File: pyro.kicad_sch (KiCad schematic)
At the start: 34 parts, among them J15 DB141R-2.54-8P-GN, Q1 MJD44H11T4G, Q10 PJM09P30DF, Q11 PJM09P30DF, Q12 PJM09P30DF, Q13 PJM09P30DF, Q4 BC817-25,215, Q5 NMOS, Q6 NMOS, Q7 NMOS, Q8 NMOS, Q9 NMOS, U7 LM334M

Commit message: perché non funziona
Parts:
- removed Q13: PJM09P30DF, easyeda2kicad:DFN-6_L2.0-W2.0-P0.65-BL-EP-1, symbol WF5803F:PJM09P30DF
- removed Q9: NMOS, Package_TO_SOT_SMD:SOT-23_Handsoldering, symbol Simulation_SPICE:NMOS
- removed R35, R37: 1k, Resistor_SMD:R_0603_1608Metric_Pad0.98x0.95mm_HandSolder, symbol Device:R_Small
- removed R36, R38: 10k, Resistor_SMD:R_0603_1608Metric_Pad0.98x0.95mm_HandSolder, symbol Device:R_Small
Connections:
- no-connect marks 20 -> 15

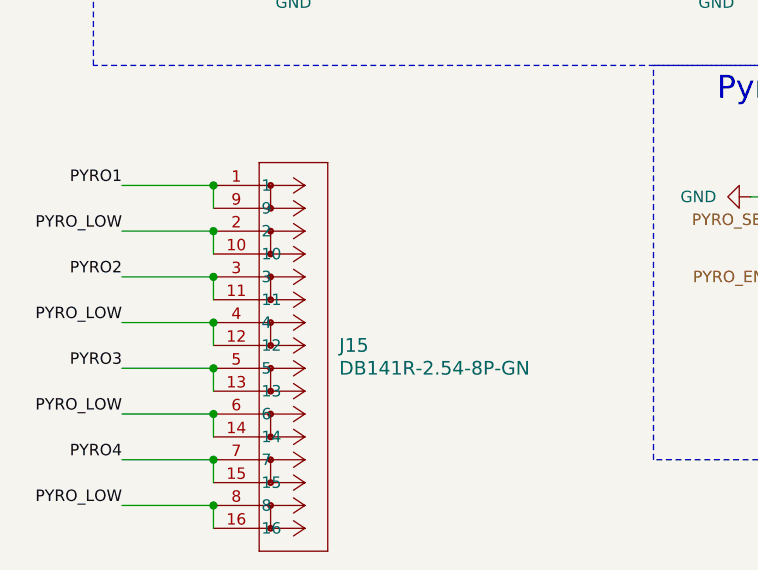
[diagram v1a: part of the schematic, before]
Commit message: spostamento connettori
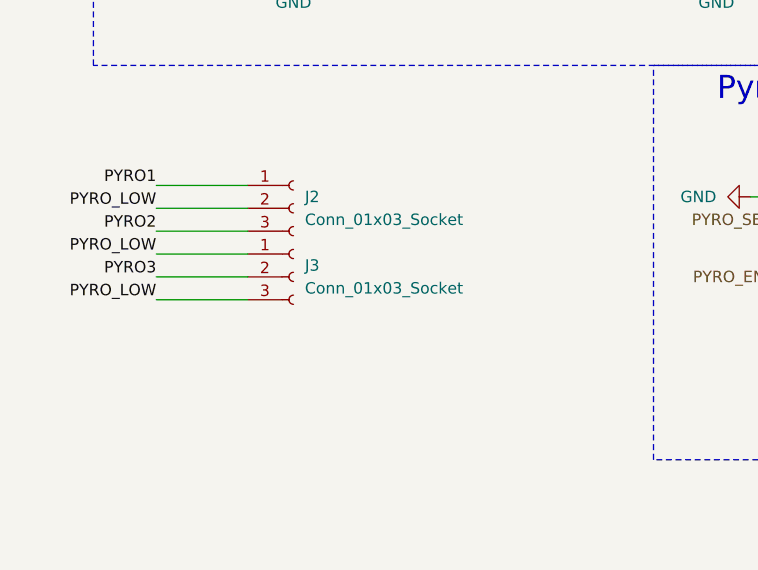
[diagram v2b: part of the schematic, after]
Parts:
- removed J15: DB141R-2.54-8P-GN, DB141R-2-54-8:CONN16_DB141R_DIO, symbol 2025-09-27_12-32-40:DB141R-2.54-8P-GN
- added J2, J3: Conn_01x03_Socket, TerminalBlock_WAGO:TerminalBlock_WAGO_2601-1103_1x03_P3.50mm_Horizontal, symbol Connector:Conn_01x03_Socket
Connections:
- net PYRO1: now also J2.1 (Pin_1)
- net PYRO2: now also J2.3 (Pin_3)
- net PYRO3: now also J3.2 (Pin_2)
- net PYRO_LOW: now also J2.2 (Pin_2), J3.1 (Pin_1), J3.3 (Pin_3)

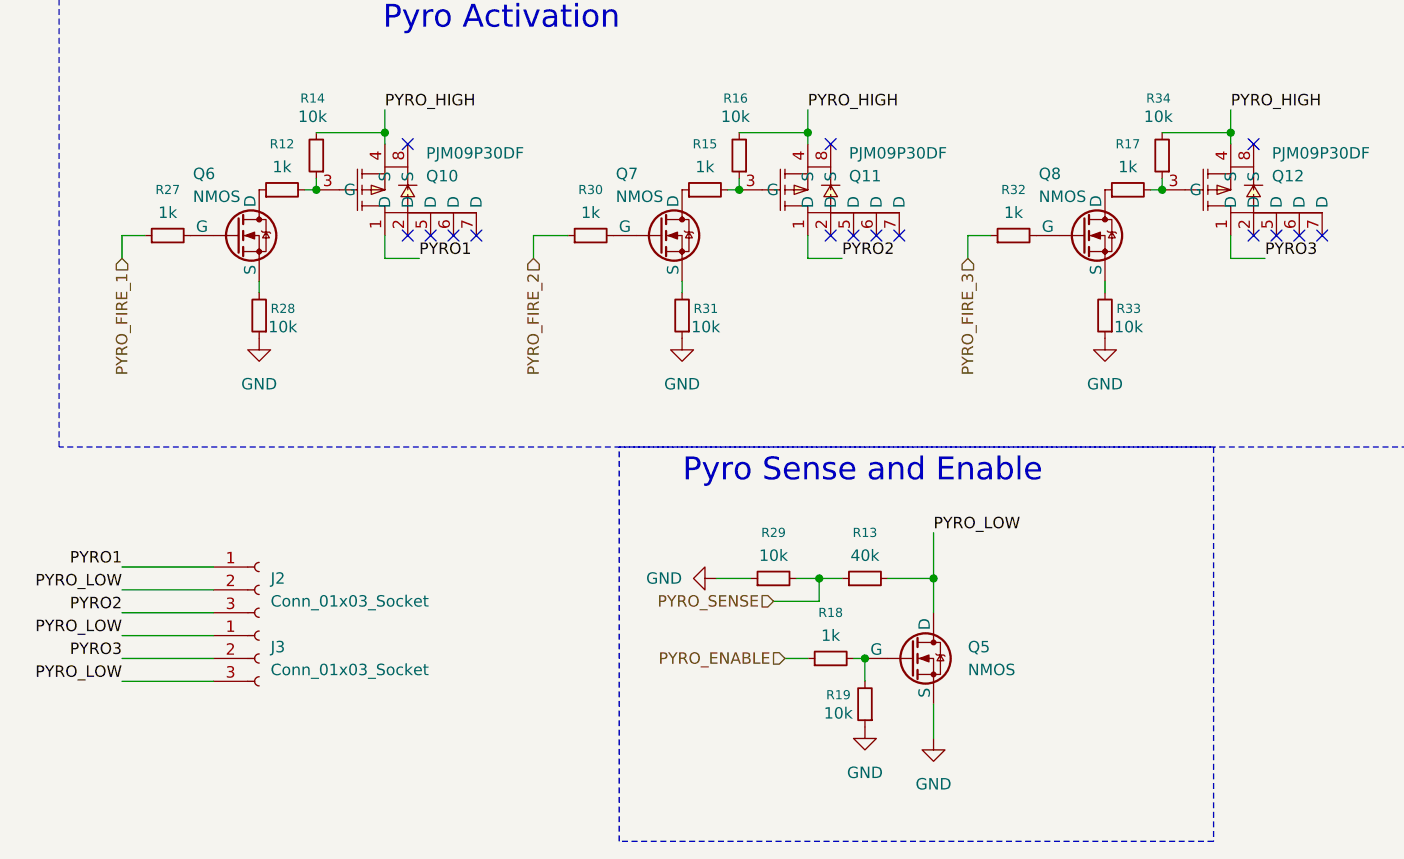
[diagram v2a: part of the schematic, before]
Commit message: connettori adattati
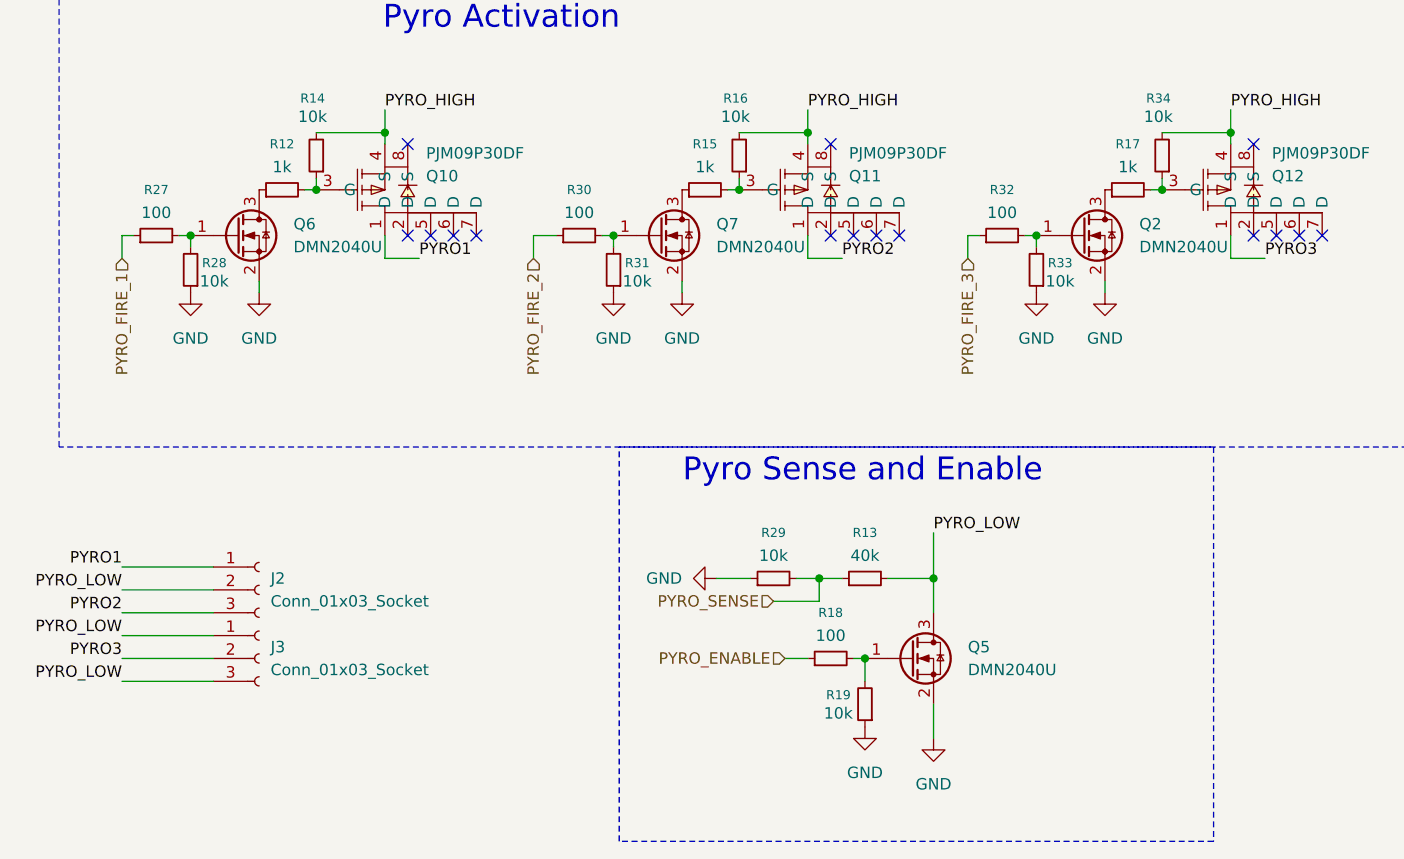
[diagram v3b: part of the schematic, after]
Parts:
- removed Q5, Q6, Q7, Q8: NMOS, Package_TO_SOT_SMD:SOT-23_Handsoldering, symbol Simulation_SPICE:NMOS
- added Q2, Q5, Q6, Q7: DMN2040U, Package_TO_SOT_SMD:SOT-23, symbol Transistor_FET:DMN2040U
- R18, R27, R30, R32: value 1k -> 100
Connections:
- net GND: now also Q2.2 (S), Q5.2 (S), Q6.2 (S), Q7.2 (S)
- net PYRO_LOW: now also Q5.3 (D)
- net at R15.1: now also Q7.3 (D)
- net at R33.2: now also R32.2, Q2.1 (G)
- net at R12.1: now also Q6.3 (D)
- net at R27.2: now also R28.2, Q6.1 (G)
- net at R18.2, R19.2: now also Q5.1 (G)
- net at R17.1: now also Q2.3 (D)
- net at R30.2: now also R31.2, Q7.1 (G)
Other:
- moved on the sheet: R27, R28, R30, R31, R32, R33

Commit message: aggiornamenti rev 1.1
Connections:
- net PYRO1: now also J2.3 (Pin_3); no longer J2.1 (Pin_1)
- net PYRO2: now also J2.1 (Pin_1); no longer J2.3 (Pin_3)
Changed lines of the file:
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@@
+		)
+	)
+	(label "PYRO2"
+		(at 58.42 128.27 180)
+		(effects
+			(font
+				(size 1.27 1.27)
+			)
+			(justify right bottom)
 		)
 	)
@@
 	)
 	(label "PYRO2"
-		(at 58.42 133.35 180)
-		(effects
-			(font
-				(size 1.27 1.27)
-			)
-			(justify right bottom)
-		)
-	)
-	(label "PYRO2"
 		(at 138.43 93.98 0)
 		(effects
@@
 	(label "PYRO3"
 		(at 58.42 138.43 180)
+		(effects
+			(font
+				(size 1.27 1.27)
+			)
+			(justify right bottom)
+		)
+	)
+	(label "PYRO1"
+		(at 58.42 133.35 180)
 		(effects
 			(font
@@
 		(effects
 			(font
-				(size 1.27 1.27)
-			)
-			(justify right bottom)
-		)
-	)
-	(label "PYRO1"
-		(at 58.42 128.27 180)
-		(effects
-			(font

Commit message: ficato connetotore wagoi se negro
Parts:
- removed J2, J3: Conn_01x03_Socket, TerminalBlock_WAGO:TerminalBlock_WAGO_2601-1103_1x03_P3.50mm_Horizontal, symbol Connector:Conn_01x03_Socket
- added J11: Conn_01x06_Pin, TerminalBlock_WAGO:TerminalBlock_WAGO_2601-1106_1x06_P3.50mm_Horizontal, symbol Connector:Conn_01x06_Pin
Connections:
- net PYRO1: now also J11.1 (Pin_1)
- net PYRO2: now also J11.3 (Pin_3)
- net PYRO3: now also J11.5 (Pin_5)
- net PYRO_LOW: now also J11.2 (Pin_2), J11.4 (Pin_4), J11.6 (Pin_6)
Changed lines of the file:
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@@
-		)
-	)
-	(label "PYRO2"
-		(at 58.42 128.27 180)
-		(effects
-			(font
-				(size 1.27 1.27)
-			)
-			(justify right bottom)
 		)
 	)
@@
 		)
 	)
+	(label "PYRO1"
+		(at 58.42 128.27 180)
+		(effects
+			(font
+				(size 1.27 1.27)
+			)
+			(justify right bottom)
+		)
+	)
 	(label "PYRO2"
 		(at 138.43 93.98 0)
@@
 		)
 	)
-	(label "PYRO3"
-		(at 58.42 138.43 180)
+	(label "PYRO2"
+		(at 58.42 133.35 180)
 		(effects
 			(font
@@
 		)
 	)
-	(label "PYRO1"
-		(at 58.42 133.35 180)
+	(label "PYRO3"
+		(at 58.42 138.43 180)
 		(effects
 			(font
@@
 	)
 	(symbol
-		(lib_id "Connector:Conn_01x03_Socket")
-		(at 73.66 130.81 0)
-		(unit 1)
-		(exclude_from_sim no)
-		(in_bom yes)
-		(on_board yes)
-		(dnp no)
-		(fields_autoplaced yes)
-		(property "Reference" "J2"
-			(at 74.93 129.5399 0)
-			(effects
-				(font
-					(size 1.27 1.27)
-				)
-				(justify left)
-			)
-		)
-		(property "Value" "Conn_01x03_Socket"
-			(at 74.93 132.0799 0)
-			(effects
-				(font
-					(size 1.27 1.27)
-				)
-				(justify left)
-			)
-		)
-		(property "Footprint" "TerminalBlock_WAGO:TerminalBlock_WAGO_2601-1103_1x03_P3.50mm_Horizontal"
-			(at 73.66 130.81 0)
-			(effects
-				(font
-					(size 1.27 1.27)
-				)
-				(hide yes)
-			)
-		)
-		(property "Datasheet" "~"
-			(at 73.66 130.81 0)
-			(effects
-				(font
-					(size 1.27 1.27)
-				)
-				(hide yes)
-			)
-		)
-		(property "Description" "Generic connector, single row, 01x03, script generated"
-			(at 73.66 130.81 0)
-			(effects
-				(font
-					(size 1.27 1.27)
-				)
-				(hide yes)
-			)
-		)
-		(pin "3"
-		)
-		(pin "2"
-		)
-		(pin "1"
-		)
-		(instances
-			(project ""
-				(path "/105f6e80-8e20-4d56-8eb3-6fa826818670/0e3bb754-11c8-4798-b0c5-c918ad2a10b9"
-					(reference "J2")
-					(unit 1)
-				)
-			)
-		)
-	)
-	(symbol
 		(lib_id "WF5803F:PJM09P30DF")
 		(at 181.61 86.36 0)
@@
 	)
 	(symbol
+		(lib_id "Connector:Conn_01x06_Pin")
+		(at 73.66 133.35 0)
+		(mirror y)
+		(unit 1)
+		(exclude_from_sim no)
+		(in_bom yes)
+		(on_board yes)
+		(dnp no)
+		(fields_autoplaced yes)
+		(property "Reference" "J11"
+			(at 74.93 133.3499 0)
+			(effects
+				(font
+					(size 1.27 1.27)
+				)
+				(justify right)
+			)
+		)
+		(property "Value" "Conn_01x06_Pin"
+			(at 74.93 135.8899 0)
+			(effects
+				(font
+					(size 1.27 1.27)
+				)
+				(justify right)
+			)
+		)
+		(property "Footprint" "TerminalBlock_WAGO:TerminalBlock_WAGO_2601-1106_1x06_P3.50mm_Horizontal"
+			(at 73.66 133.35 0)
+			(effects
+				(font
+					(size 1.27 1.27)
+				)
+				(hide yes)
+			)
+		)
+		(property "Datasheet" "~"
+			(at 73.66 133.35 0)
+			(effects
+				(font
+					(size 1.27 1.27)
+				)
+				(hide yes)
+			)
+		)
+		(property "Description" "Generic connector, single row, 01x06, script generated"
+			(at 73.66 133.35 0)
+			(effects
+				(font
+					(size 1.27 1.27)
+				)
+				(hide yes)
+			)
+		)
+		(pin "2"
+		)
+		(pin "6"
+		)
+		(pin "1"
+		)
+		(pin "3"
+		)
+		(pin "4"
+		)
+		(pin "5"
+		)
+		(instances
+			(project ""
+				(path "/105f6e80-8e20-4d56-8eb3-6fa826818670/0e3bb754-11c8-4798-b0c5-c918ad2a10b9"
+					(reference "J11")
+					(unit 1)
+				)
+			)
+		)
+	)
+	(symbol
 		(lib_id "Device:R_Small")
 		(at 130.81 129.54 90)
@@
 					(unit 1)
 				)
-			)
-		)
-	)
-	(symbol
-		(lib_id "Connector:Conn_01x03_Socket")
-		(at 73.66 138.43 0)
-		(unit 1)
-		(exclude_from_sim no)
-		(in_bom yes)
-		(on_board yes)
-		(dnp no)
-		(fields_autoplaced yes)
-		(property "Reference" "J3"
-			(at 74.93 137.1599 0)
-			(effects
-				(font
-					(size 1.27 1.27)
-				)
-				(justify left)
-			)
-		)
-		(property "Value" "Conn_01x03_Socket"
-			(at 74.93 139.6999 0)
-			(effects
-				(font
-					(size 1.27 1.27)
-				)
-				(justify left)
-			)
-		)
-		(property "Footprint" "TerminalBlock_WAGO:TerminalBlock_WAGO_2601-1103_1x03_P3.50mm_Horizontal"
-			(at 73.66 138.43 0)
-			(effects
-				(font
-					(size 1.27 1.27)
-				)
-				(hide yes)
-			)
-		)
-		(property "Datasheet" "~"
-			(at 73.66 138.43 0)
-			(effects
-				(font
-					(size 1.27 1.27)
-				)
-				(hide yes)
-			)
-		)
-		(property "Description" "Generic connector, single row, 01x03, script generated"
-			(at 73.66 138.43 0)
-			(effects
-				(font
-					(size 1.27 1.27)
-				)
-				(hide yes)
-			)
-		)
-		(pin "3"
-		)
-		(pin "2"
-		)
-		(pin "1"
-		)
-		(instances
-			(project "TABv1"
-				(path "/105f6e80-8e20-4d56-8eb3-6fa826818670/0e3bb754-11c8-4798-b0c5-c918ad2a10b9"
-					(reference "J3")
-					(unit 1)
-				)

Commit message: Ordered
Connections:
- net PYRO1: now also Q10.2 (D), Q10.5 (D), Q10.6 (D), Q10.7 (D)
- net PYRO2: now also Q11.2 (D), Q11.5 (D), Q11.6 (D), Q11.7 (D)
- net PYRO3: now also Q12.2 (D), Q12.5 (D), Q12.6 (D), Q12.7 (D)
- net PYRO_HIGH: now also Q10.8 (S), Q11.8 (S), Q12.8 (S)
- no-connect marks 15 -> 0
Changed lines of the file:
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@@
+	)
+	(junction
+		(at 95.25 91.44)
+		(diameter 0)
+		(color 0 0 0 0)
+	)
+	(junction
+		(at 184.15 91.44)
+		(diameter 0)
+		(color 0 0 0 0)
+	)
+	(junction
+		(at 92.71 91.44)
+		(diameter 0)
+		(color 0 0 0 0)
+	)
+	(junction
+		(at 181.61 91.44)
+		(diameter 0)
+		(color 0 0 0 0)
 	)
 	(junction
@@
 	)
 	(junction
+		(at 134.62 91.44)
+		(diameter 0)
+		(color 0 0 0 0)
+	)
+	(junction
+		(at 186.69 91.44)
+		(diameter 0)
+		(color 0 0 0 0)
+	)
+	(junction
 		(at 80.01 86.36)
 		(diameter 0)
@@
 	)
 	(junction
+		(at 87.63 91.44)
+		(diameter 0)
+		(color 0 0 0 0)
+	)
+	(junction
 		(at 140.97 138.43)
 		(diameter 0)
@@
 	)
 	(junction
+		(at 139.7 91.44)
+		(diameter 0)
+		(color 0 0 0 0)
+	)
+	(junction
 		(at 87.63 80.01)
 		(diameter 0)
@@
 	)
 	(junction
+		(at 90.17 91.44)
+		(diameter 0)
+		(color 0 0 0 0)
+	)
+	(junction
+		(at 137.16 91.44)
+		(diameter 0)
+		(color 0 0 0 0)
+	)
+	(junction
+		(at 189.23 91.44)
+		(diameter 0)
+		(color 0 0 0 0)
+	)
+	(junction
 		(at 160.02 91.44)
 		(diameter 0)
@@
 	)
 	(junction
+		(at 142.24 91.44)
+		(diameter 0)
+		(color 0 0 0 0)
+	)
+	(junction
 		(at 181.61 80.01)
 		(diameter 0)
@@
 		(color 0 0 0 0)
 	)
-	(no_connect
-		(at 90.17 81.28)
-	)
-	(no_connect
-		(at 184.15 81.28)
-	)
-	(no_connect
-		(at 142.24 91.44)
-	)
-	(no_connect
-		(at 184.15 91.44)
-	)
-	(no_connect
-		(at 186.69 91.44)
-	)
-	(no_connect
-		(at 137.16 91.44)
-	)
-	(no_connect
-		(at 92.71 91.44)
-	)
-	(no_connect
-		(at 137.16 81.28)
-	)
-	(no_connect
-		(at 95.25 91.44)
-	)
-	(no_connect
-		(at 191.77 91.44)
-	)
-	(no_connect
-		(at 189.23 91.44)
-	)
-	(no_connect
-		(at 97.79 91.44)
-	)
-	(no_connect
-		(at 144.78 91.44)
-	)
-	(no_connect
-		(at 90.17 91.44)
-	)
-	(no_connect
-		(at 139.7 91.44)
-	)
 	(wire
 		(pts
@@
 	(wire
 		(pts
-			(xy 87.63 93.98) (xy 91.44 93.98)
+			(xy 87.63 100.33) (xy 91.44 100.33)
+		)
+		(stroke
+			(width 0)
+			(type default)
+		)
+	)
+	(wire
+		(pts
+			(xy 137.16 80.01) (xy 137.16 81.28)
 		)
 		(stroke
@@
 		)
 	)
+	(wire
+		(pts
+			(xy 142.24 91.44) (xy 144.78 91.44)
+		)
+		(stroke
+			(width 0)
+			(type default)
+		)
+	)
 	(polyline
 		(pts
@@
 	(wire
 		(pts
+			(xy 134.62 80.01) (xy 137.16 80.01)
+		)
+		(stroke
+			(width 0)
+			(type default)
+		)
+	)
+	(wire
+		(pts
+			(xy 139.7 91.44) (xy 142.24 91.44)
+		)
+		(stroke
+			(width 0)
+			(type default)
+		)
+	)
+	(wire
+		(pts
+			(xy 92.71 91.44) (xy 95.25 91.44)
+		)
+		(stroke
+			(width 0)
+			(type default)
+		)
+	)
+	(wire
+		(pts
 			(xy 132.08 138.43) (xy 134.62 138.43)
 		)
@@
 	(wire
 		(pts
+			(xy 189.23 91.44) (xy 191.77 91.44)
+		)
+		(stroke
+			(width 0)
+			(type default)
+		)
+	)
+	(wire
+		(pts
 			(xy 66.04 92.71) (xy 66.04 91.44)
 		)
@@
 	(wire
 		(pts
+			(xy 95.25 91.44) (xy 97.79 91.44)
+		)
+		(stroke
+			(width 0)
+			(type default)
+		)
+	)
+	(wire
+		(pts
+			(xy 184.15 80.01) (xy 184.15 81.28)
+		)
+		(stroke
+			(width 0)
+			(type default)
+		)
+	)
+	(wire
+		(pts
 			(xy 87.63 77.47) (xy 87.63 80.01)
 		)
@@
 	(wire
 		(pts
+			(xy 181.61 91.44) (xy 184.15 91.44)
+		)
+		(stroke
+			(width 0)
+			(type default)
+		)
+	)
+	(wire
+		(pts
 			(xy 78.74 86.36) (xy 80.01 86.36)
 		)
@@
 	(wire
 		(pts
+			(xy 87.63 80.01) (xy 90.17 80.01)
+		)
+		(stroke
+			(width 0)
+			(type default)
+		)
+	)
+	(wire
+		(pts
+			(xy 137.16 91.44) (xy 139.7 91.44)
+		)
+		(stroke
+			(width 0)
+			(type default)
+		)
+	)
+	(wire
+		(pts
 			(xy 153.67 50.8) (xy 153.67 52.07)
 		)
@@
 		)
 	)
+	(wire
+		(pts
+			(xy 134.62 91.44) (xy 137.16 91.44)
+		)
+		(stroke
+			(width 0)
+			(type default)
+		)
+	)
 	(polyline
 		(pts
@@
 	(wire
 		(pts
+			(xy 90.17 80.01) (xy 90.17 81.28)
+		)
+		(stroke
+			(width 0)
+			(type default)
+		)
+	)
+	(wire
+		(pts
 			(xy 153.67 33.02) (xy 153.67 34.29)
 		)
@@
 	(wire
 		(pts
-			(xy 181.61 93.98) (xy 185.42 93.98)
+			(xy 181.61 99.06) (xy 185.42 99.06)
 		)
 		(stroke
@@
 	(wire
 		(pts
-			(xy 181.61 91.44) (xy 181.61 93.98)
+			(xy 181.61 91.44) (xy 181.61 99.06)
 		)
 		(stroke
@@
 	(wire
 		(pts
+			(xy 87.63 91.44) (xy 90.17 91.44)
+		)
+		(stroke
+			(width 0)
+			(type default)
+		)
+	)
+	(wire
+		(pts
 			(xy 58.42 133.35) (xy 68.58 133.35)
 		)
@@
 	(wire
 		(pts
-			(xy 87.63 91.44) (xy 87.63 93.98)
+			(xy 87.63 91.44) (xy 87.63 100.33)
 		)
 		(stroke
@@
 	(wire
 		(pts
+			(xy 184.15 91.44) (xy 186.69 91.44)
+		)
+		(stroke
+			(width 0)
+			(type default)
+		)
+	)
+	(wire
+		(pts
 			(xy 139.7 138.43) (xy 140.97 138.43)
 		)
@@
 	(wire
 		(pts
+			(xy 186.69 91.44) (xy 189.23 91.44)
+		)
+		(stroke
+			(width 0)
+			(type default)
+		)
+	)
+	(wire
+		(pts
 			(xy 80.01 80.01) (xy 87.63 80.01)
 		)
@@
 	(wire
 		(pts
-			(xy 134.62 93.98) (xy 138.43 93.98)
+			(xy 134.62 100.33) (xy 138.43 100.33)
 		)
 		(stroke
@@
 	(wire
 		(pts
+			(xy 90.17 91.44) (xy 92.71 91.44)
+		)
+		(stroke
+			(width 0)
+			(type default)
+		)
+	)
+	(wire
+		(pts
+			(xy 181.61 80.01) (xy 184.15 80.01)
+		)
+		(stroke
+			(width 0)
+			(type default)
+		)
+	)
+	(wire
+		(pts
 			(xy 153.67 52.07) (xy 167.64 52.07)
 		)
@@
 	(wire
 		(pts
-			(xy 134.62 91.44) (xy 134.62 93.98)
+			(xy 134.62 91.44) (xy 134.62 100.33)
 		)
 		(stroke
@@
 	)
 	(label "PYRO3"
-		(at 185.42 93.98 0)
+		(at 185.42 99.06 0)
 		(effects
 			(font
@@
 	)
 	(label "PYRO2"
-		(at 138.43 93.98 0)
+		(at 138.43 100.33 0)
 		(effects
 			(font
@@
 	)
 	(label "PYRO1"
-		(at 91.44 93.98 0)
+		(at 91.44 100.33 0)
 		(effects
 			(font
